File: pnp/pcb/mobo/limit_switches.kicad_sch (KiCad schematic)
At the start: 12 parts, among them J2 X_LIMIT, J3 Y_LIMIT, J4 Z_LIMIT, J5 L_LIMIT, J6 R_LIMIT, J7 A_LIMIT

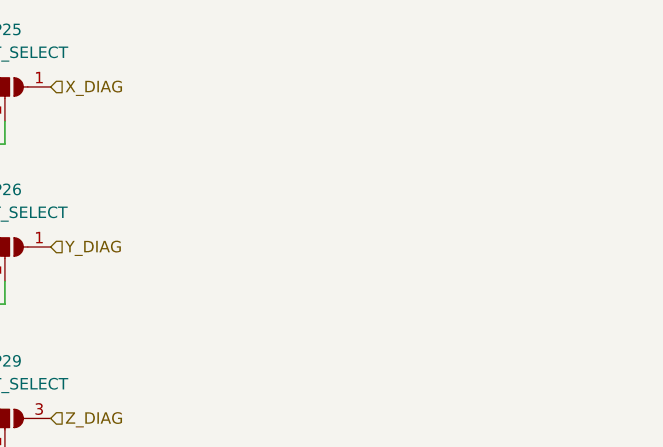
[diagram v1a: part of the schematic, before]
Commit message: Redesign finished
Completed Board redesign and adding more EMC improvements.
Changed all the part numbers to have a Mouser orderable design (except the JST connectors)
All outputs generated
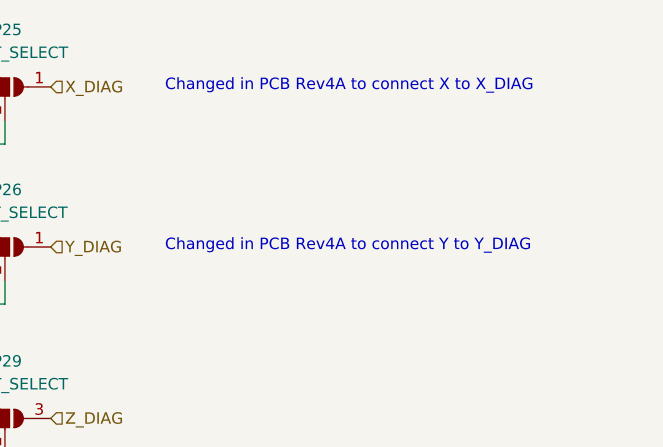
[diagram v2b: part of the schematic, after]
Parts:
- J2, J3, J4, J5, J6, J7: JLCPCB C2316 -> (none); LCSC C2316 -> (none); Mouser (none) -> Digikey
- JP25, JP26, JP29, JP30, JP31, JP32: Mouser (none) -> -
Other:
- note added: "Changed in PCB Rev4A to connect X to X_DIAG"
- note added: "Changed in PCB Rev4A to connect Y to Y_DIAG"
- company: Opulo -> Opulo.io
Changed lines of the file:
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@@
   (title_block
     (title "LumenPnP Motherboard")
-    (date "2022-09-09")
-    (rev "004A")
-    (company "Opulo")
+    (date "2022-10-06")
+    (rev "04A")
+    (company "Opulo.io")
     (comment 1 "Reengineered by Magpie")
   )
@@
   (wire (pts (xy 189.23 128.27) (xy 189.23 125.73))
     (stroke (width 0) (type default) (color 0 0 0 0))
+  )
+  (text "Changed in PCB Rev4A to connect Y to Y_DIAG" (at 207.01 86.995 0)
+    (effects (font (size 1.27 1.27)) (justify left bottom))
+  )
+  (text "Changed in PCB Rev4A to connect X to X_DIAG" (at 207.01 69.215 0)
+    (effects (font (size 1.27 1.27)) (justify left bottom))
   )
   (label "X_LIMIT" (at 147.32 86.36 180)
@@
       (effects (font (size 1.27 1.27)) hide)
     )
+    (property "Mouser" "-" (id 4) (at 189.23 86.36 0)
+      (effects (font (size 1.27 1.27)) hide)
+    )
     (pin "1")
     (pin "2")
@@
       (effects (font (size 1.27 1.27)) hide)
     )
-    (property "LCSC" "C2316" (id 4) (at 152.4 93.98 0)
-      (effects (font (size 1.27 1.27)) hide)
-    )
-    (property "JLCPCB" "C2316" (id 5) (at 152.4 93.98 0)
+    (property "LCSC" "" (id 4) (at 152.4 93.98 0)
+      (effects (font (size 1.27 1.27)) hide)
+    )
+    (property "JLCPCB" "" (id 5) (at 152.4 93.98 0)
       (effects (font (size 1.27 1.27)) hide)
     )
@@
       (effects (font (size 1.27 1.27)) hide)
     )
+    (property "Mouser" "Digikey" (id 7) (at 152.4 93.98 0)
+      (effects (font (size 1.27 1.27)) hide)
+    )
     (pin "1")
     (pin "2")
@@
       (effects (font (size 1.27 1.27)) hide)
     )
-    (property "LCSC" "C2316" (id 4) (at 152.4 124.46 0)
-      (effects (font (size 1.27 1.27)) hide)
-    )
-    (property "JLCPCB" "C2316" (id 5) (at 152.4 124.46 0)
+    (property "LCSC" "" (id 4) (at 152.4 124.46 0)
+      (effects (font (size 1.27 1.27)) hide)
+    )
+    (property "JLCPCB" "" (id 5) (at 152.4 124.46 0)
       (effects (font (size 1.27 1.27)) hide)
     )
@@
       (effects (font (size 1.27 1.27)) hide)
     )
+    (property "Mouser" "Digikey" (id 7) (at 152.4 124.46 0)
+      (effects (font (size 1.27 1.27)) hide)
+    )
     (pin "1")
     (pin "2")
@@
       (effects (font (size 1.27 1.27)) hide)
     )
-    (property "LCSC" "C2316" (id 4) (at 152.4 83.82 0)
-      (effects (font (size 1.27 1.27)) hide)
-    )
-    (property "JLCPCB" "C2316" (id 5) (at 152.4 83.82 0)
+    (property "LCSC" "" (id 4) (at 152.4 83.82 0)
+      (effects (font (size 1.27 1.27)) hide)
+    )
+    (property "JLCPCB" "" (id 5) (at 152.4 83.82 0)
       (effects (font (size 1.27 1.27)) hide)
     )
     (property "Digikey" "455-2248-ND" (id 6) (at 152.4 83.82 0)
+      (effects (font (size 1.27 1.27)) hide)
+    )
+    (property "Mouser" "Digikey" (id 7) (at 152.4 83.82 0)
       (effects (font (size 1.27 1.27)) hide)
     )
@@
       (effects (font (size 1.27 1.27)) hide)
     )
+    (property "Mouser" "-" (id 4) (at 189.23 121.92 0)
+      (effects (font (size 1.27 1.27)) hide)
+    )
     (pin "1")
     (pin "2")
@@
       (effects (font (size 1.27 1.27)) hide)
     )
+    (property "Mouser" "-" (id 4) (at 189.23 68.58 0)
+      (effects (font (size 1.27 1.27)) hide)
+    )
     (pin "1")
     (pin "2")
@@
       (effects (font (size 1.27 1.27)) hide)
     )
+    (property "Mouser" "-" (id 4) (at 189.23 105.41 0)
+      (effects (font (size 1.27 1.27)) hide)
+    )
     (pin "1")
     (pin "2")
@@
       (effects (font (size 1.27 1.27)) hide)
     )
-    (property "LCSC" "C2316" (id 4) (at 152.4 134.62 0)
-      (effects (font (size 1.27 1.27)) hide)
-    )
-    (property "JLCPCB" "C2316" (id 5) (at 152.4 134.62 0)
+    (property "LCSC" "" (id 4) (at 152.4 134.62 0)
+      (effects (font (size 1.27 1.27)) hide)
+    )
+    (property "JLCPCB" "" (id 5) (at 152.4 134.62 0)
       (effects (font (size 1.27 1.27)) hide)
     )
     (property "Digikey" "455-2248-ND" (id 6) (at 152.4 134.62 0)
+      (effects (font (size 1.27 1.27)) hide)
+    )
+    (property "Mouser" "Digikey" (id 7) (at 152.4 134.62 0)
       (effects (font (size 1.27 1.27)) hide)
     )
@@
       (effects (font (size 1.27 1.27)) hide)
     )
+    (property "Mouser" "-" (id 4) (at 189.23 156.21 0)
+      (effects (font (size 1.27 1.27)) hide)
+    )
     (pin "1")
     (pin "2")
@@
       (effects (font (size 1.27 1.27)) hide)
     )
-    (property "LCSC" "C2316" (id 4) (at 152.4 104.14 0)
-      (effects (font (size 1.27 1.27)) hide)
-    )
-    (property "JLCPCB" "C2316" (id 5) (at 152.4 104.14 0)
+    (property "LCSC" "" (id 4) (at 152.4 104.14 0)
+      (effects (font (size 1.27 1.27)) hide)
+    )
+    (property "JLCPCB" "" (id 5) (at 152.4 104.14 0)
       (effects (font (size 1.27 1.27)) hide)
     )
@@
       (effects (font (size 1.27 1.27)) hide)
     )
+    (property "Mouser" "Digikey" (id 7) (at 152.4 104.14 0)
+      (effects (font (size 1.27 1.27)) hide)
+    )
     (pin "1")
     (pin "2")
@@
       (effects (font (size 1.27 1.27)) hide)
     )
-    (property "LCSC" "C2316" (id 4) (at 152.4 114.3 0)
-      (effects (font (size 1.27 1.27)) hide)
-    )
-    (property "JLCPCB" "C2316" (id 5) (at 152.4 114.3 0)
+    (property "LCSC" "" (id 4) (at 152.4 114.3 0)
+      (effects (font (size 1.27 1.27)) hide)
+    )
+    (property "JLCPCB" "" (id 5) (at 152.4 114.3 0)
       (effects (font (size 1.27 1.27)) hide)
     )
     (property "Digikey" "455-2248-ND" (id 6) (at 152.4 114.3 0)
+      (effects (font (size 1.27 1.27)) hide)
+    )
+    (property "Mouser" "Digikey" (id 7) (at 152.4 114.3 0)
       (effects (font (size 1.27 1.27)) hide)
     )
@@
       (effects (font (size 1.27 1.27)) hide)
     )
+    (property "Mouser" "-" (id 4) (at 189.23 139.7 0)
+      (effects (font (size 1.27 1.27)) hide)
+    )
